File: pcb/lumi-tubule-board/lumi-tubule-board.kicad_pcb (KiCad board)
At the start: 2 copper layers, 83.1 x 83 mm, 42 parts, among them SW1 SWITCH_TACT_SMT4.6X2.8, SW2 SWITCH_TACT_SMT4.6X2.8, U1 SHTC3, U2 VREG_SOT23-5, U3 ESP32-S3-MINI-1, U4 LIS2Dx12, U5 TLC59108xPW, U6 TLC59108xPW, X1 USB_C

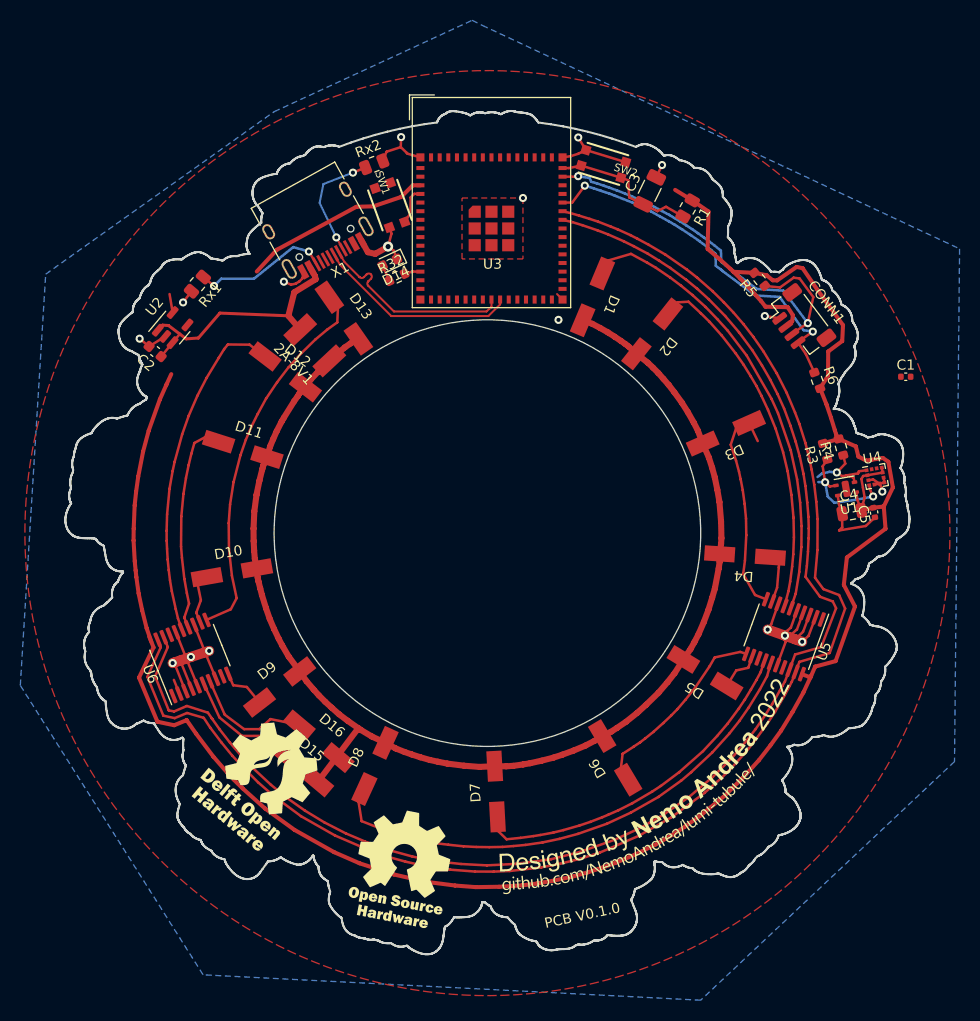
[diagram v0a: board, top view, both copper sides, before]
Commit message: Complete TLC59018 implementaiton
Fully routed board which should theoretically need only cosmetic alterations. Some issues with soldermask goign outside the board (might cause manufacturer to get upset).
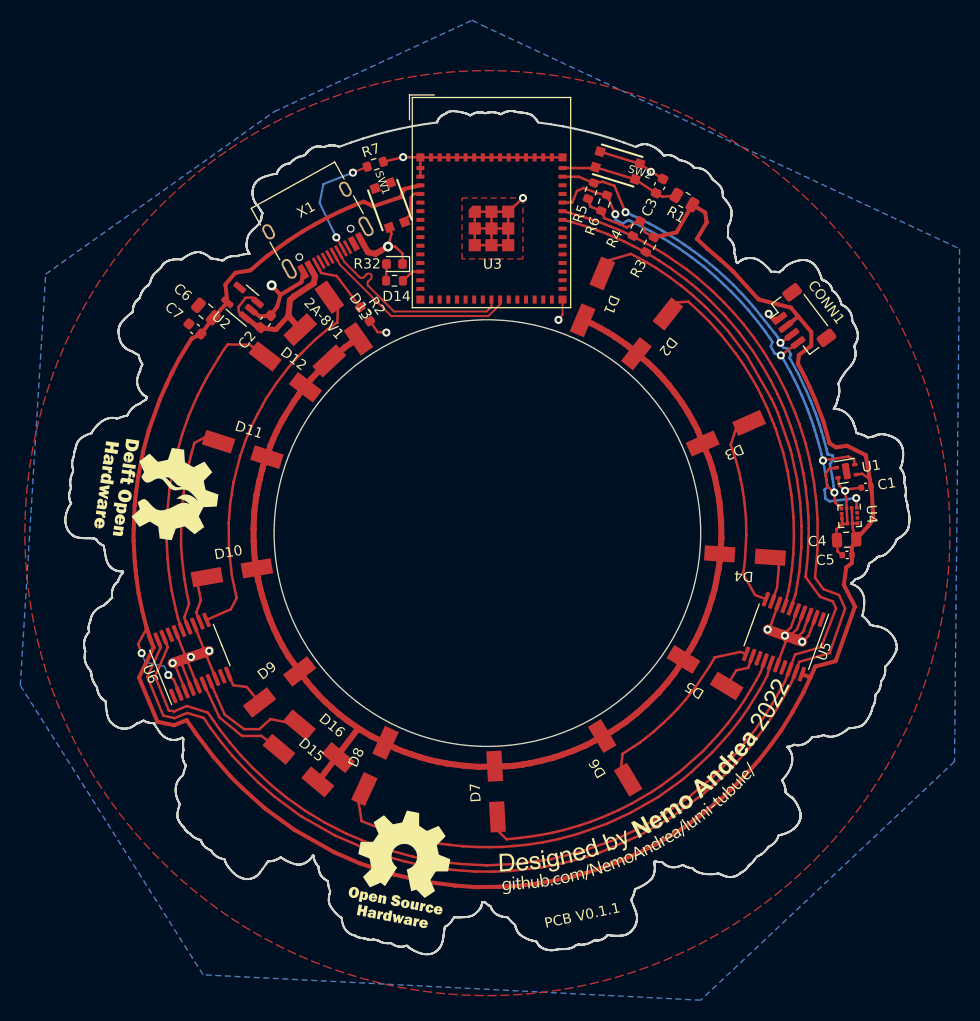
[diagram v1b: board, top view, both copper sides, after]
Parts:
- removed Rx1, Rx2: 5.1K, Resistor_SMD:R_0805_2012Metric
- added C6: 10uF, Capacitor_SMD:C_0805_2012Metric, F.Cu at (122.3, 78.2)
- added C7: 1uF, Capacitor_SMD:C_0603_1608Metric, F.Cu at (121.2, 79.9)
- added R2: 5.1k, Resistor_SMD:R_0603_1608Metric, F.Cu at (137.9, 78.5)
- added R7: 5.1k, Resistor_SMD:R_0603_1608Metric, F.Cu at (138.9, 63.7)
- C2: value 22uF -> 10uF
- C3: footprint Capacitor_SMD:C_1206_3216Metric -> Capacitor_SMD:C_0603_1608Metric
- moved R4 29.5 mm to (164.7, 70.0), turned to -117 degrees
- moved R6 27.3 mm to (161.5, 67.5), turned to 70 degrees
- moved R3 26.7 mm to (166.0, 71.6), turned to -119 degrees
- moved R5 18.7 mm to (160.2, 66.3), turned to 70 degrees
- moved C1 11.5 mm to (187.3, 95.5), turned to 9 degrees
- moved C2 11.3 mm to (128.2, 79.2), turned to -130 degrees
- moved U2 7.31 mm to (125.9, 77.3), turned to 140 degrees
- moved C5 4.95 mm to (185.4, 102.2), turned to 3 degrees
- moved U4 4.65 mm to (185.7, 98.3), turned to -87 degrees
- moved C4 2.77 mm to (185.4, 100.7), turned to 3 degrees
- moved U1 1.74 mm to (185.3, 93.9), turned to -170.5 degrees
- moved SW2 1.41 mm to (162.8, 63.8)
- moved C3 1.07 mm to (166.9, 65.8)
- moved R1 0.88 mm to (169.4, 67.2), turned to 150 degrees
- moved D14 0.49 mm to (140.8, 73.5), turned to 180 degrees
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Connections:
- C2 pad 1: Net-(2A-8V1-Pad2) -> GND
- C2 pad 2: GND -> Net-(2A-8V1-Pad2)
- U3 pad 61: Net-(U3-Pad61) -> GND
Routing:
- net GND: track 84.5 -> 124.6 mm, vias 17 -> 15
- net /3.3V: track 227.5 -> 238.8 mm, vias 0 -> 2
- net SCL: track 44.4 -> 55.1 mm, vias 2 -> 4
- net Net-(2A-8V1-Pad2): track 25.4 -> 16.9 mm
- net Net-(X1-PadB5): track 13.6 -> 6.38 mm, vias 2 -> 0
- net Net-(C3-Pad1): track 14.4 -> 11.9 mm
- net Net-(D3-Pad1): track 21.5 -> 19.5 mm
- net Net-(R32-Pad2): track 1.58 -> 2.09 mm
- net SCL_int: track 141.7 -> 141.6 mm, vias 1 -> 0
- net SDA: vias 2 -> 3
- net SDA_int: vias 2 -> 0
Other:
- outline, holes or cut-outs redrawn
- board text added: "PCB V0.1.1"
- board text removed: "PCB V0.1.0"
